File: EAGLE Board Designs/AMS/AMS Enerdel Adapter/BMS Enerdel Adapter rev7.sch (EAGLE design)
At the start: 134 parts, among them J1 CONNECTOR-1_5222_, J10 CONNECTOR-1_5222_, J11 CONNECTOR-1_5222_, J12 CONNECTOR-1_5222_, J13 CONNECTOR-1_5222_, J14 CONNECTOR-1_5222_, J15 CONNECTOR-1_5222_, J16 CONNECTOR-1_5222_, J17 CONNECTOR-1_5222_, J18 CONNECTOR-1_5222_, J19 CONNECTOR-1_5222_, J2 CONNECTOR-1_5222_, J20 CONNECTOR-1_5222_, J21 CONNECTOR-1_5222_, J22 CONNECTOR-1_5222_, J3 CONNECTOR-1_5222_, J4 CONNECTOR-1_5222_, J5 CONNECTOR-1_5222_, J6 CONNECTOR-1_5222_, J7 CONNECTOR-1_5222_, J8 CONNECTOR-1_5222_, J9 CONNECTOR-1_5222_

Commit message: Update BMS Enerdel Adapter rev7.sch
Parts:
- removed A-UPPER-OUT-14, A_LOWER_IN-1, A_LOWER_IN-10, A_LOWER_IN-11, A_LOWER_IN-12, A_LOWER_IN-13', A_LOWER_IN-14, A_LOWER_IN-2, A_LOWER_IN-3, A_LOWER_IN-4, A_LOWER_IN-5, A_LOWER_IN-6, A_LOWER_IN-7, A_LOWER_IN-8, A_LOWER_IN-9, A_LOWER_OUT-1, A_LOWER_OUT-10, A_LOWER_OUT-11, A_LOWER_OUT-12, A_LOWER_OUT-13, A_LOWER_OUT-14, A_LOWER_OUT-2, A_LOWER_OUT-3, A_LOWER_OUT-4, A_LOWER_OUT-5, A_LOWER_OUT-6, A_LOWER_OUT-7, A_LOWER_OUT-8, A_LOWER_OUT-9, A_UPPER_IN-1, A_UPPER_IN-10, A_UPPER_IN-11, A_UPPER_IN-12, A_UPPER_IN-13, A_UPPER_IN-14, A_UPPER_IN-2, A_UPPER_IN-3, A_UPPER_IN-4, A_UPPER_IN-5, A_UPPER_IN-6, A_UPPER_IN-7, A_UPPER_IN-8, A_UPPER_IN-9, A_UPPER_OUT-1, A_UPPER_OUT-10, A_UPPER_OUT-11, A_UPPER_OUT-12, A_UPPER_OUT-13, A_UPPER_OUT-2, A_UPPER_OUT-3, A_UPPER_OUT-4, A_UPPER_OUT-5, A_UPPER_OUT-6, A_UPPER_OUT-7, A_UPPER_OUT-8, A_UPPER_OUT-9, B_LOWER_IN-1, B_LOWER_IN-10, B_LOWER_IN-11, B_LOWER_IN-12, B_LOWER_IN-13, B_LOWER_IN-14, B_LOWER_IN-2, B_LOWER_IN-3, B_LOWER_IN-4, B_LOWER_IN-5, B_LOWER_IN-6, B_LOWER_IN-7, B_LOWER_IN-8, B_LOWER_IN-9, B_LOWER_OUT-1, B_LOWER_OUT-10, B_LOWER_OUT-11, B_LOWER_OUT-12, B_LOWER_OUT-13, B_LOWER_OUT-14, B_LOWER_OUT-2, B_LOWER_OUT-3, B_LOWER_OUT-4, B_LOWER_OUT-5, B_LOWER_OUT-6, B_LOWER_OUT-7, B_LOWER_OUT-8, B_LOWER_OUT-9, B_UPPER_IN-1, B_UPPER_IN-10, B_UPPER_IN-11, B_UPPER_IN-12, B_UPPER_IN-13, B_UPPER_IN-14, B_UPPER_IN-2, B_UPPER_IN-3, B_UPPER_IN-4, B_UPPER_IN-5, B_UPPER_IN-6, B_UPPER_IN-7, B_UPPER_IN-8, B_UPPER_IN-9, B_UPPER_OUT-1, B_UPPER_OUT-10, B_UPPER_OUT-11, B_UPPER_OUT-12, B_UPPER_OUT-13, B_UPPER_OUT-14, B_UPPER_OUT-2, B_UPPER_OUT-3, B_UPPER_OUT-4, B_UPPER_OUT-5, B_UPPER_OUT-6, B_UPPER_OUT-7, B_UPPER_OUT-8, B_UPPER_OUT-9: CONNECTOR-1_POGO_, HyTechDevices:CONNECTOR-1_POGO_
- added A_LOWER_IN, A_LOWER_OUT, A_UPPER_IN, A_UPPER_OUT, B_LOWER_IN, B_LOWER_OUT, B_UPPER_IN, B_UPPER_OUT: CONNECTOR-14, HyTechDevices:CONNECTOR-14
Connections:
- removed net N$23: A_UPPER_IN-13.1, A_UPPER_OUT-13.1
- removed net N$24: A_UPPER_IN-12.1, A_UPPER_OUT-12.1
- removed net N$27: A_UPPER_IN-9.1, A_UPPER_OUT-9.1
- removed net N$59: B_LOWER_IN-3.1, B_LOWER_OUT-3.1
- removed net N$60: B_LOWER_IN-2.1, B_LOWER_OUT-2.1
- removed net N$61: B_LOWER_IN-1.1, B_LOWER_OUT-1.1
- net A1-B7: now also A_LOWER_IN-1.S, A_LOWER_OUT-1.S, B_LOWER_IN-4.S, B_LOWER_OUT-4.S; no longer A_LOWER_IN-1.1, A_LOWER_OUT-1.1, B_LOWER_IN-4.1, B_LOWER_OUT-4.1
- net A10-B16: now also A_LOWER_IN-10.S, A_LOWER_OUT-10.S, B_LOWER_IN-13.S, B_LOWER_OUT-13.S, B_UPPER_IN-1.S, B_UPPER_OUT-1.S; no longer A_LOWER_IN-10.1, A_LOWER_OUT-10.1, B_LOWER_IN-13.1, B_LOWER_OUT-13.1, B_UPPER_IN-1.1, B_UPPER_OUT-1.1
- net A11-B17: now also A_LOWER_IN-11.S, A_LOWER_OUT-11.S, B_UPPER_IN-2.S, B_UPPER_OUT-2.S; no longer A_LOWER_IN-11.1, A_LOWER_OUT-11.1, B_UPPER_IN-2.1, B_UPPER_OUT-2.1
- net A12-B18: now also A_LOWER_IN-12.S, A_LOWER_OUT-12.S, A_UPPER_IN-12.S, A_UPPER_OUT-12.S, B_UPPER_IN-3.S, B_UPPER_OUT-3.S; no longer A_LOWER_IN-12.1, A_LOWER_OUT-12.1, B_UPPER_IN-3.1, B_UPPER_OUT-3.1
- net A13-B19: now also A_LOWER_IN-13.S, A_LOWER_OUT-13.S, A_UPPER_IN-1.S, A_UPPER_IN-13.S, A_UPPER_OUT-1.S, A_UPPER_OUT-13.S, B_LOWER_IN-1.S, B_LOWER_OUT-1.S, B_UPPER_IN-4.S, B_UPPER_OUT-4.S; no longer A_LOWER_IN-13'.1, A_LOWER_OUT-13.1, A_UPPER_IN-1.1, A_UPPER_OUT-1.1, B_UPPER_IN-4.1, B_UPPER_OUT-4.1
- net A14-B20: now also A_UPPER_IN-2.S, A_UPPER_OUT-2.S, B_LOWER_IN-2.S, B_LOWER_OUT-2.S, B_UPPER_IN-5.S, B_UPPER_OUT-5.S; no longer A_UPPER_IN-2.1, A_UPPER_OUT-2.1, B_UPPER_IN-5.1, B_UPPER_OUT-5.1
- net A15-B21: now also A_UPPER_IN-3.S, A_UPPER_OUT-3.S, B_LOWER_IN-3.S, B_LOWER_OUT-3.S, B_UPPER_IN-6.S, B_UPPER_OUT-6.S; no longer A_UPPER_IN-3.1, A_UPPER_OUT-3.1, B_UPPER_IN-6.1, B_UPPER_OUT-6.1
- net A16-B22: now also A_UPPER_IN-4.S, A_UPPER_OUT-4.S, B_UPPER_IN-7.S, B_UPPER_OUT-7.S; no longer A_UPPER_IN-4.1, A_UPPER_OUT-4.1, B_UPPER_IN-7.1, B_UPPER_OUT-7.1
- net A17-B23: now also A_UPPER_IN-5.S, A_UPPER_OUT-5.S, B_UPPER_IN-8.S, B_UPPER_OUT-8.S; no longer A_UPPER_IN-5.1, A_UPPER_OUT-5.1, B_UPPER_IN-8.1, B_UPPER_OUT-8.1
- net A18-B24: now also A_UPPER_IN-6.S, A_UPPER_OUT-6.S, B_UPPER_IN-9.S, B_UPPER_OUT-9.S; no longer A_UPPER_IN-6.1, A_UPPER_OUT-6.1, B_UPPER_IN-9.1, B_UPPER_OUT-9.1
- net A19-B25: now also A_UPPER_IN-8.S, A_UPPER_OUT-8.S, B_UPPER_IN-10.S, B_UPPER_OUT-10.S; no longer A_UPPER_IN-7.1, A_UPPER_OUT-7.1, B_UPPER_IN-10.1, B_UPPER_OUT-10.1
- net A2-B8: now also A_LOWER_IN-2.S, A_LOWER_OUT-2.S, B_LOWER_IN-5.S, B_LOWER_OUT-5.S; no longer A_LOWER_IN-2.1, A_LOWER_OUT-2.1, B_LOWER_IN-5.1, B_LOWER_OUT-5.1
- net A20-B26: now also A_UPPER_IN-9.S, A_UPPER_OUT-9.S, B_UPPER_IN-11.S, B_UPPER_OUT-11.S; no longer A_UPPER_IN-8.1, A_UPPER_OUT-8.1, B_UPPER_IN-11.1, B_UPPER_OUT-11.1
- net A21-B27: now also A_UPPER_IN-10.S, A_UPPER_OUT-10.S, B_UPPER_IN-12.S, B_UPPER_OUT-12.S; no longer A_UPPER_IN-10.1, A_UPPER_OUT-10.1, B_UPPER_IN-12.1, B_UPPER_OUT-12.1
- net A22-B28: now also A_UPPER_IN-11.S, A_UPPER_OUT-11.S, B_UPPER_IN-13.S, B_UPPER_OUT-13.S; no longer A_UPPER_IN-11.1, A_UPPER_OUT-11.1, B_UPPER_IN-13.1, B_UPPER_OUT-13.1
- net A3-B9: now also A_LOWER_IN-3.S, A_LOWER_OUT-3.S, B_LOWER_IN-6.S, B_LOWER_OUT-6.S; no longer A_LOWER_IN-3.1, A_LOWER_OUT-3.1, B_LOWER_IN-6.1, B_LOWER_OUT-6.1
- net A4-B10: now also A_LOWER_IN-4.S, A_LOWER_OUT-4.S, B_LOWER_IN-7.S, B_LOWER_OUT-7.S; no longer A_LOWER_IN-4.1, A_LOWER_OUT-4.1, B_LOWER_IN-7.1, B_LOWER_OUT-7.1
- net A5-B11: now also A_LOWER_IN-5.S, A_LOWER_OUT-5.S, B_LOWER_IN-8.S, B_LOWER_OUT-8.S; no longer A_LOWER_IN-5.1, A_LOWER_OUT-5.1, B_LOWER_IN-8.1, B_LOWER_OUT-8.1
- net A6-B12: now also A_LOWER_IN-6.S, A_LOWER_OUT-6.S, B_LOWER_IN-9.S, B_LOWER_OUT-9.S; no longer A_LOWER_IN-6.1, A_LOWER_OUT-6.1, B_LOWER_IN-9.1, B_LOWER_OUT-9.1
- net A7-B13: now also A_LOWER_IN-7.S, A_LOWER_OUT-7.S, A_UPPER_IN-7.S, A_UPPER_OUT-7.S, B_LOWER_IN-10.S, B_LOWER_OUT-10.S; no longer A_LOWER_IN-7.1, A_LOWER_OUT-7.1, B_LOWER_IN-10.1, B_LOWER_OUT-10.1
- net A8-B14: now also A_LOWER_IN-8.S, A_LOWER_OUT-8.S, B_LOWER_IN-11.S, B_LOWER_OUT-11.S; no longer A_LOWER_IN-8.1, A_LOWER_OUT-8.1, B_LOWER_IN-11.1, B_LOWER_OUT-11.1
- net A9-B15: now also A_LOWER_IN-9.S, A_LOWER_OUT-9.S, B_LOWER_IN-12.S, B_LOWER_OUT-12.S; no longer A_LOWER_IN-9.1, A_LOWER_OUT-9.1, B_LOWER_IN-12.1, B_LOWER_OUT-12.1

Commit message: Finished rev 7 schematic
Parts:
- removed A_LOWER_IN, A_LOWER_OUT, A_UPPER_IN, A_UPPER_OUT, B_LOWER_IN, B_LOWER_OUT, B_UPPER_IN, B_UPPER_OUT: CONNECTOR-14, HyTechDevices:CONNECTOR-14
- added A-CONNECTOR-14-LOWER-IN, A-CONNECTOR-14-LOWER-OUT, B-CONNECTOR-14-LOWER-IN, B-CONNECTOR-14-LOWER-OUT: CONNECTOR-14_MINIFIT_, HyTechDevices:CONNECTOR-14_MINIFIT_
- added A-CONNECTOR-14-UPPER-IN, A-CONNECTOR-14-UPPER-OUT, B-CONNECTOR-14-UPPER-IN, B-CONNECTOR-14-UPPER-OUT: CONNECTOR-14_NANOFIT_, HyTechDevices:CONNECTOR-14_NANOFIT_
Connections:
- new net N$2: A-CONNECTOR-14-UPPER-IN.13, A-CONNECTOR-14-UPPER-OUT.13
- new net N$3: A-CONNECTOR-14-UPPER-IN.12, A-CONNECTOR-14-UPPER-OUT.12
- new net N$8: A-CONNECTOR-14-UPPER-IN.7, A-CONNECTOR-14-UPPER-OUT.7
- net A1-B7: now also A-CONNECTOR-14-LOWER-IN.1, A-CONNECTOR-14-LOWER-OUT.1, B-CONNECTOR-14-LOWER-IN.1, B-CONNECTOR-14-LOWER-IN.4, B-CONNECTOR-14-LOWER-OUT.1, B-CONNECTOR-14-LOWER-OUT.4; no longer A_LOWER_IN-1.S, A_LOWER_OUT-1.S, B_LOWER_IN-4.S, B_LOWER_OUT-4.S
- net A10-B16: now also A-CONNECTOR-14-LOWER-IN.10, A-CONNECTOR-14-LOWER-OUT.10, B-CONNECTOR-14-LOWER-IN.13, B-CONNECTOR-14-LOWER-OUT.13, B-CONNECTOR-14-UPPER-IN.1, B-CONNECTOR-14-UPPER-OUT.1; no longer A_LOWER_IN-10.S, A_LOWER_OUT-10.S, B_LOWER_IN-13.S, B_LOWER_OUT-13.S, B_UPPER_IN-1.S, B_UPPER_OUT-1.S
- net A11-B17: now also A-CONNECTOR-14-LOWER-IN.11, A-CONNECTOR-14-LOWER-OUT.11, B-CONNECTOR-14-UPPER-IN.2, B-CONNECTOR-14-UPPER-OUT.2; no longer A_LOWER_IN-11.S, A_LOWER_OUT-11.S, B_UPPER_IN-2.S, B_UPPER_OUT-2.S
- net A12-B18: now also A-CONNECTOR-14-LOWER-IN.12, A-CONNECTOR-14-LOWER-OUT.12, B-CONNECTOR-14-UPPER-IN.3, B-CONNECTOR-14-UPPER-OUT.3; no longer A_LOWER_IN-12.S, A_LOWER_OUT-12.S, A_UPPER_IN-12.S, A_UPPER_OUT-12.S, B_UPPER_IN-3.S, B_UPPER_OUT-3.S
- net A13-B19: now also A-CONNECTOR-14-LOWER-IN.13, A-CONNECTOR-14-LOWER-OUT.13, A-CONNECTOR-14-UPPER-IN.1, A-CONNECTOR-14-UPPER-OUT.1, B-CONNECTOR-14-UPPER-IN.4, B-CONNECTOR-14-UPPER-OUT.4; no longer A_LOWER_IN-13.S, A_LOWER_OUT-13.S, A_UPPER_IN-1.S, A_UPPER_IN-13.S, A_UPPER_OUT-1.S, A_UPPER_OUT-13.S, B_LOWER_IN-1.S, B_LOWER_OUT-1.S, B_UPPER_IN-4.S, B_UPPER_OUT-4.S
- net A14-B20: now also A-CONNECTOR-14-UPPER-IN.2, A-CONNECTOR-14-UPPER-OUT.2, B-CONNECTOR-14-UPPER-IN.5, B-CONNECTOR-14-UPPER-OUT.5; no longer A_UPPER_IN-2.S, A_UPPER_OUT-2.S, B_LOWER_IN-2.S, B_LOWER_OUT-2.S, B_UPPER_IN-5.S, B_UPPER_OUT-5.S
- net A15-B21: now also A-CONNECTOR-14-UPPER-IN.3, A-CONNECTOR-14-UPPER-OUT.3, B-CONNECTOR-14-UPPER-IN.6, B-CONNECTOR-14-UPPER-OUT.6; no longer A_UPPER_IN-3.S, A_UPPER_OUT-3.S, B_LOWER_IN-3.S, B_LOWER_OUT-3.S, B_UPPER_IN-6.S, B_UPPER_OUT-6.S
- net A16-B22: now also A-CONNECTOR-14-UPPER-IN.4, A-CONNECTOR-14-UPPER-OUT.4, B-CONNECTOR-14-UPPER-IN.7, B-CONNECTOR-14-UPPER-OUT.7; no longer A_UPPER_IN-4.S, A_UPPER_OUT-4.S, B_UPPER_IN-7.S, B_UPPER_OUT-7.S
- net A17-B23: now also A-CONNECTOR-14-UPPER-IN.5, A-CONNECTOR-14-UPPER-OUT.5, B-CONNECTOR-14-UPPER-IN.8, B-CONNECTOR-14-UPPER-OUT.8; no longer A_UPPER_IN-5.S, A_UPPER_OUT-5.S, B_UPPER_IN-8.S, B_UPPER_OUT-8.S
- net A18-B24: now also A-CONNECTOR-14-UPPER-IN.6, A-CONNECTOR-14-UPPER-OUT.6, B-CONNECTOR-14-UPPER-IN.9, B-CONNECTOR-14-UPPER-OUT.9; no longer A_UPPER_IN-6.S, A_UPPER_OUT-6.S, B_UPPER_IN-9.S, B_UPPER_OUT-9.S
- net A19-B25: now also A-CONNECTOR-14-UPPER-IN.8, A-CONNECTOR-14-UPPER-OUT.8, B-CONNECTOR-14-UPPER-IN.10, B-CONNECTOR-14-UPPER-OUT.10; no longer A_UPPER_IN-8.S, A_UPPER_OUT-8.S, B_UPPER_IN-10.S, B_UPPER_OUT-10.S
- net A2-B8: now also A-CONNECTOR-14-LOWER-IN.2, A-CONNECTOR-14-LOWER-OUT.2, B-CONNECTOR-14-LOWER-IN.2, B-CONNECTOR-14-LOWER-IN.5, B-CONNECTOR-14-LOWER-OUT.2, B-CONNECTOR-14-LOWER-OUT.5; no longer A_LOWER_IN-2.S, A_LOWER_OUT-2.S, B_LOWER_IN-5.S, B_LOWER_OUT-5.S
- net A20-B26: now also A-CONNECTOR-14-UPPER-IN.9, A-CONNECTOR-14-UPPER-OUT.9, B-CONNECTOR-14-UPPER-IN.11, B-CONNECTOR-14-UPPER-OUT.11; no longer A_UPPER_IN-9.S, A_UPPER_OUT-9.S, B_UPPER_IN-11.S, B_UPPER_OUT-11.S
- net A21-B27: now also A-CONNECTOR-14-UPPER-IN.10, A-CONNECTOR-14-UPPER-OUT.10, B-CONNECTOR-14-UPPER-IN.12, B-CONNECTOR-14-UPPER-OUT.12; no longer A_UPPER_IN-10.S, A_UPPER_OUT-10.S, B_UPPER_IN-12.S, B_UPPER_OUT-12.S
- net A22-B28: now also A-CONNECTOR-14-UPPER-IN.11, A-CONNECTOR-14-UPPER-OUT.11, B-CONNECTOR-14-UPPER-IN.13, B-CONNECTOR-14-UPPER-OUT.13; no longer A_UPPER_IN-11.S, A_UPPER_OUT-11.S, B_UPPER_IN-13.S, B_UPPER_OUT-13.S
- net A3-B9: now also A-CONNECTOR-14-LOWER-IN.3, A-CONNECTOR-14-LOWER-OUT.3, B-CONNECTOR-14-LOWER-IN.3, B-CONNECTOR-14-LOWER-IN.6, B-CONNECTOR-14-LOWER-OUT.3, B-CONNECTOR-14-LOWER-OUT.6; no longer A_LOWER_IN-3.S, A_LOWER_OUT-3.S, B_LOWER_IN-6.S, B_LOWER_OUT-6.S
- net A4-B10: now also A-CONNECTOR-14-LOWER-IN.4, A-CONNECTOR-14-LOWER-OUT.4, A-CONNECTOR-14-UPPER-OUT.14, B-CONNECTOR-14-LOWER-IN.7, B-CONNECTOR-14-LOWER-OUT.7; no longer A_LOWER_IN-4.S, A_LOWER_OUT-4.S, B_LOWER_IN-7.S, B_LOWER_OUT-7.S
- net A5-B11: now also A-CONNECTOR-14-LOWER-IN.5, A-CONNECTOR-14-LOWER-OUT.5, B-CONNECTOR-14-LOWER-IN.8, B-CONNECTOR-14-LOWER-OUT.8; no longer A_LOWER_IN-5.S, A_LOWER_OUT-5.S, B_LOWER_IN-8.S, B_LOWER_OUT-8.S
- net A6-B12: now also A-CONNECTOR-14-LOWER-IN.6, A-CONNECTOR-14-LOWER-OUT.6, B-CONNECTOR-14-LOWER-IN.9, B-CONNECTOR-14-LOWER-OUT.9; no longer A_LOWER_IN-6.S, A_LOWER_OUT-6.S, B_LOWER_IN-9.S, B_LOWER_OUT-9.S
- net A7-B13: now also A-CONNECTOR-14-LOWER-IN.7, A-CONNECTOR-14-LOWER-OUT.7, B-CONNECTOR-14-LOWER-IN.10, B-CONNECTOR-14-LOWER-OUT.10; no longer A_LOWER_IN-7.S, A_LOWER_OUT-7.S, A_UPPER_IN-7.S, A_UPPER_OUT-7.S, B_LOWER_IN-10.S, B_LOWER_OUT-10.S
- net A8-B14: now also A-CONNECTOR-14-LOWER-IN.8, A-CONNECTOR-14-LOWER-OUT.8, B-CONNECTOR-14-LOWER-IN.11, B-CONNECTOR-14-LOWER-OUT.11; no longer A_LOWER_IN-8.S, A_LOWER_OUT-8.S, B_LOWER_IN-11.S, B_LOWER_OUT-11.S
- net A9-B15: now also A-CONNECTOR-14-LOWER-IN.9, A-CONNECTOR-14-LOWER-OUT.9, B-CONNECTOR-14-LOWER-IN.12, B-CONNECTOR-14-LOWER-OUT.12; no longer A_LOWER_IN-9.S, A_LOWER_OUT-9.S, B_LOWER_IN-12.S, B_LOWER_OUT-12.S

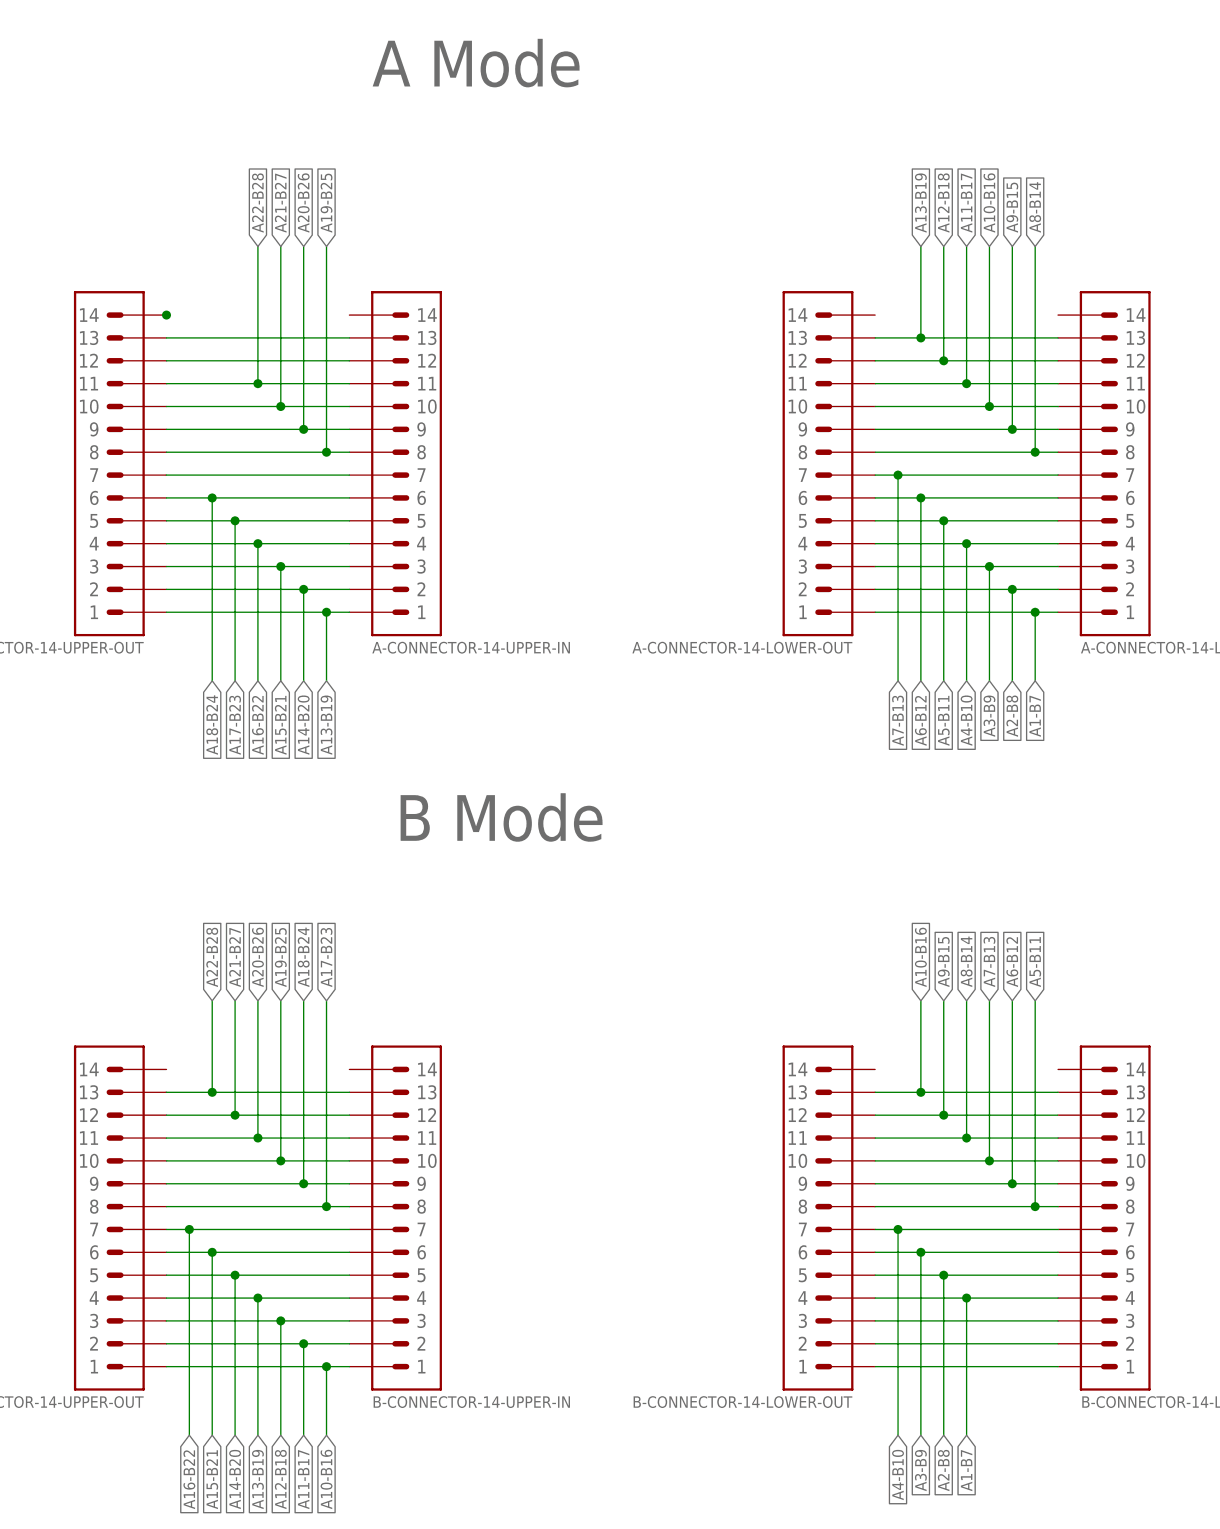
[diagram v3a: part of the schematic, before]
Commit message: Schematic Framework Finished
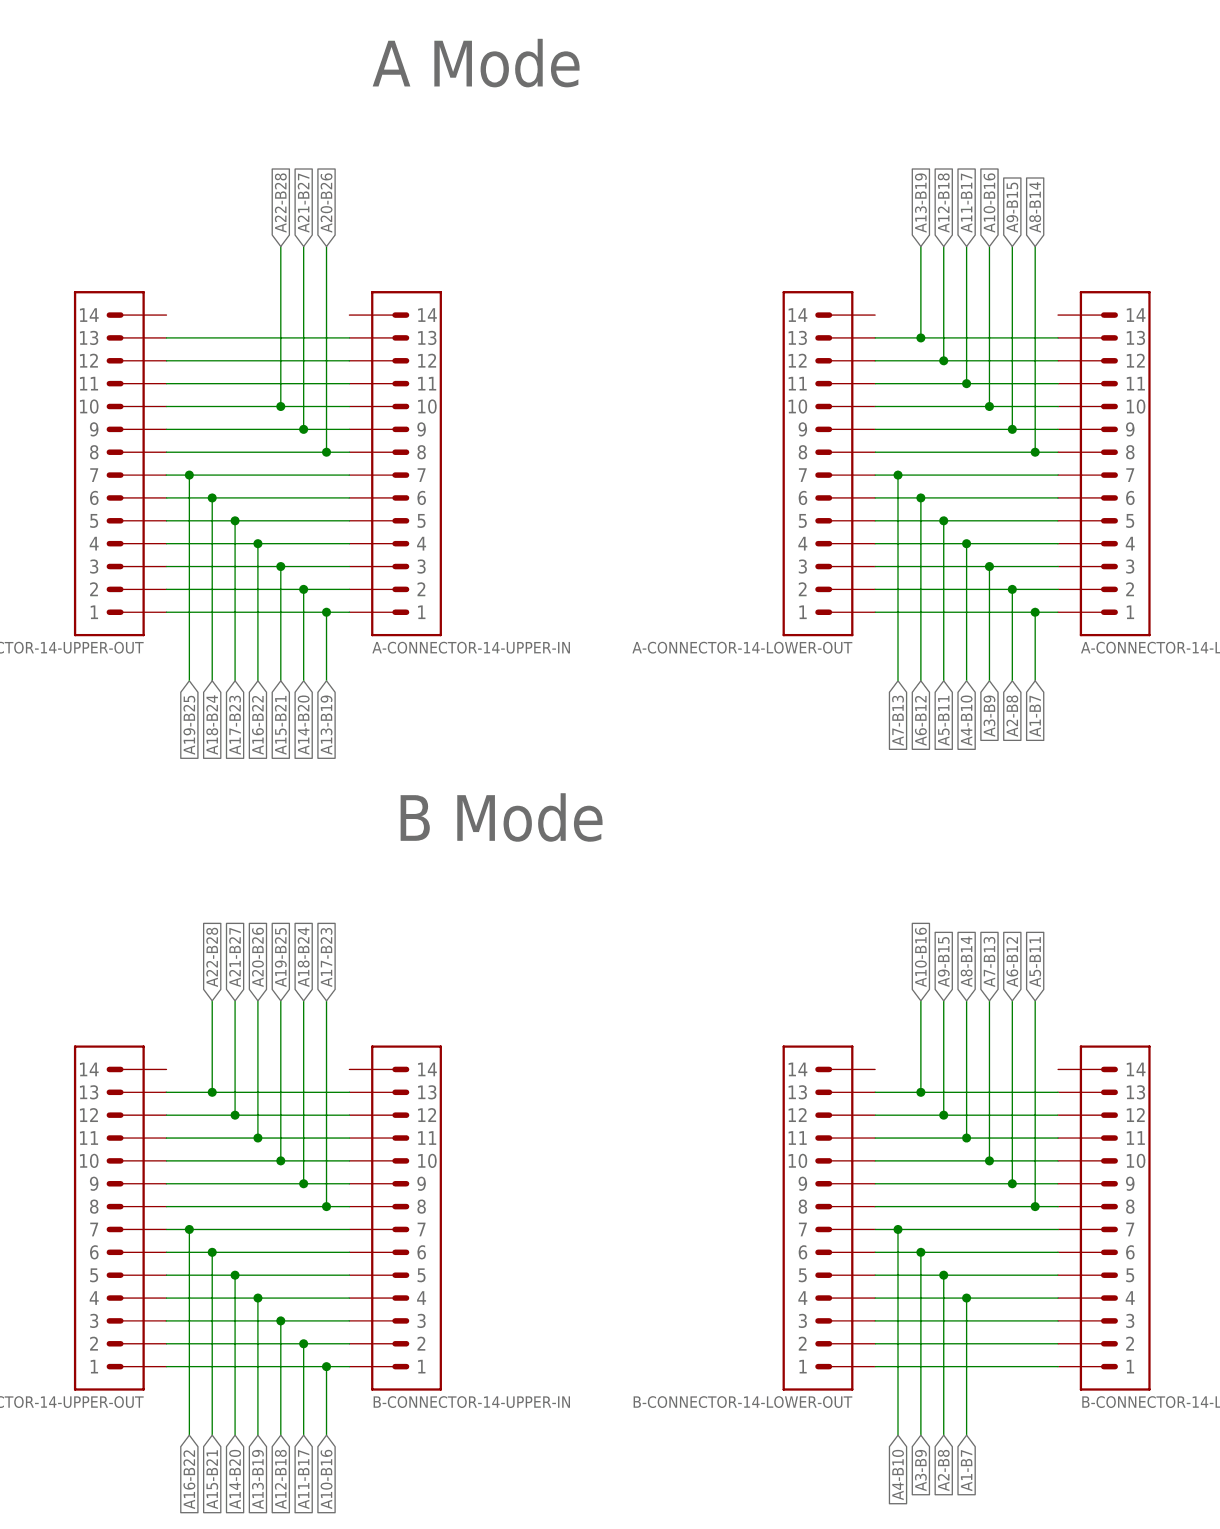
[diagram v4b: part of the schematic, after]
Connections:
- removed net N$8: A-CONNECTOR-14-UPPER-IN.7, A-CONNECTOR-14-UPPER-OUT.7
- new net B-PASS1: B-CONNECTOR-14-LOWER-IN.3, B-CONNECTOR-14-LOWER-OUT.3
- new net B-PASS2: B-CONNECTOR-14-LOWER-IN.2, B-CONNECTOR-14-LOWER-OUT.2
- new net B-PASS3: B-CONNECTOR-14-LOWER-IN.1, B-CONNECTOR-14-LOWER-OUT.1
- new net N$5: A-CONNECTOR-14-UPPER-IN.11, A-CONNECTOR-14-UPPER-OUT.11
- net A1-B7: no longer B-CONNECTOR-14-LOWER-IN.1, B-CONNECTOR-14-LOWER-OUT.1
- net A19-B25: now also A-CONNECTOR-14-UPPER-IN.7, A-CONNECTOR-14-UPPER-OUT.7; no longer A-CONNECTOR-14-UPPER-IN.8, A-CONNECTOR-14-UPPER-OUT.8
- net A2-B8: no longer B-CONNECTOR-14-LOWER-IN.2, B-CONNECTOR-14-LOWER-OUT.2
- net A20-B26: now also A-CONNECTOR-14-UPPER-IN.8, A-CONNECTOR-14-UPPER-OUT.8; no longer A-CONNECTOR-14-UPPER-IN.9, A-CONNECTOR-14-UPPER-OUT.9
- net A21-B27: now also A-CONNECTOR-14-UPPER-IN.9, A-CONNECTOR-14-UPPER-OUT.9; no longer A-CONNECTOR-14-UPPER-IN.10, A-CONNECTOR-14-UPPER-OUT.10
- net A22-B28: now also A-CONNECTOR-14-UPPER-IN.10, A-CONNECTOR-14-UPPER-OUT.10; no longer A-CONNECTOR-14-UPPER-IN.11, A-CONNECTOR-14-UPPER-OUT.11
- net A3-B9: no longer B-CONNECTOR-14-LOWER-IN.3, B-CONNECTOR-14-LOWER-OUT.3
- net A4-B10: no longer A-CONNECTOR-14-UPPER-OUT.14
